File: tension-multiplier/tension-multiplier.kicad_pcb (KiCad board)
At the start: 2 copper layers, 23 x 16 mm, 4 parts, among them J1 Conn_01x03_Pin, J2 Conn_01x02_Pin, J3 Conn_01x02_Pin, U1 AD633ARZ

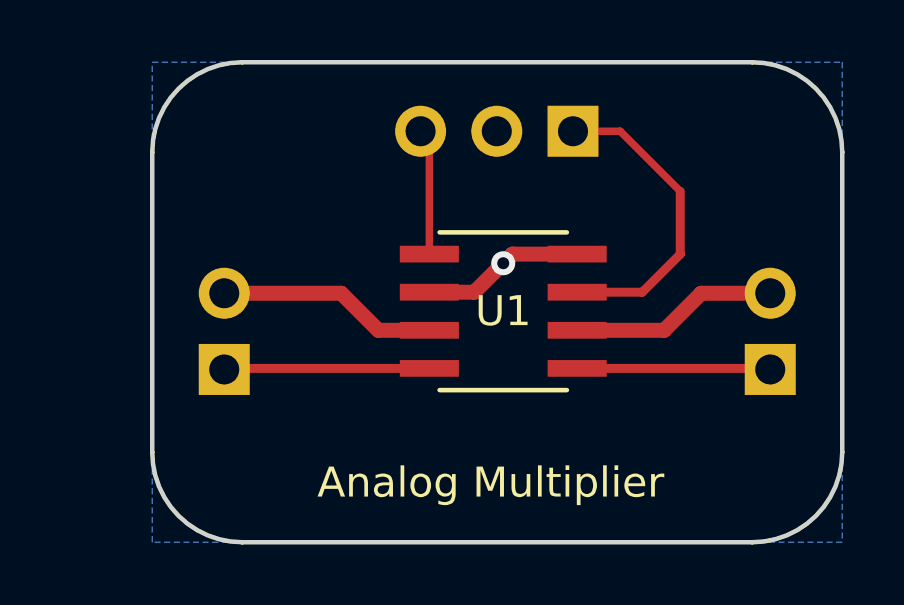
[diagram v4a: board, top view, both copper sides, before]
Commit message: Modifies auxiliary boards
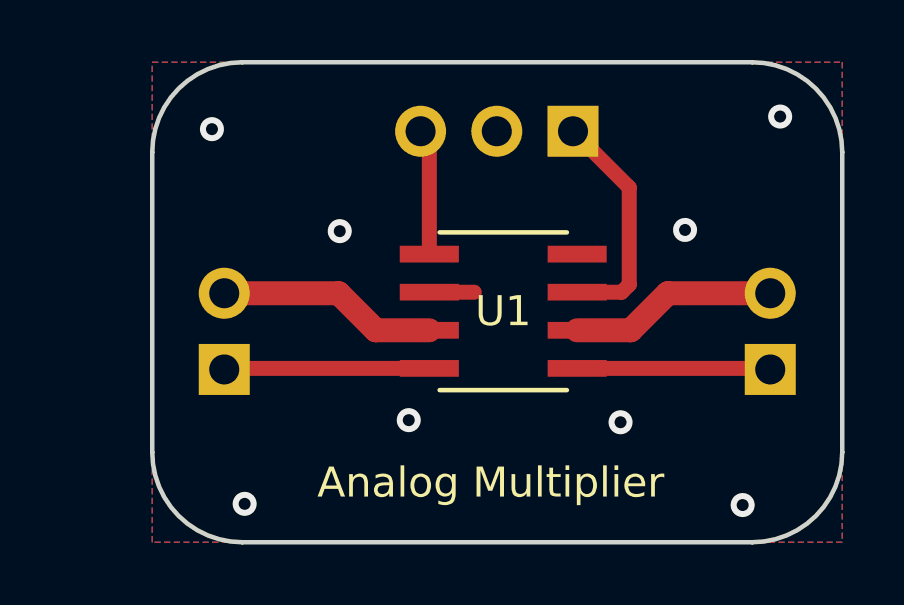
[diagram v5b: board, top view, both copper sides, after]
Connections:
- net VDD renamed +9V
- net VEE renamed -9V
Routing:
- net GND: track 5.76 -> 1.80 mm, vias 1 -> 8
- net Net-(J1-Pin_1): track 10.5 -> 7.73 mm
- added copper zone on F.Cu, net GND
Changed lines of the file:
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@@
       (outputformat 1)
       (mirror false)
-      (drillshape 1)
+      (drillshape 0)
       (scaleselection 1)
-      (outputdirectory "")
+      (outputdirectory "gerber_files")
     )
   )
@@
   (net 3 "Net-(J2-Pin_1)")
   (net 4 "Net-(J3-Pin_1)")
-  (net 5 "VDD")
-  (net 6 "GND")
-  (net 7 "VEE")
+  (net 5 "GND")
+  (net 6 "-9V")
+  (net 7 "+9V")
   (footprint "footprints:R_8_ADI" (layer "F.Cu")
     (at 149.7 88.3)
@@
     (attr smd)
     (fp_text reference "U1" (at 0 0 unlocked) (layer "F.SilkS")
-        (effects (font (size 1 1) (thickness 0.2)))
+        (effects (font (size 1 1) (thickness 0.15)))
     )
     (fp_text value "AD633ARZ" (at 0 0 unlocked) (layer "F.Fab")
-        (effects (font (size 1 1) (thickness 0.2)))
+        (effects (font (size 1 1) (thickness 0.15)))
     )
     (fp_text user "*" (at -2.7178 -3.606 unlocked) (layer "F.SilkS") hide
@@
         (effects (font (size 1 1) (thickness 0.15)))
     )
+    (fp_text user "*" (at -1.6129 -2.4257 unlocked) (layer "F.Fab")
+        (effects (font (size 1 1) (thickness 0.15)))
+    )
+    (fp_text user "*" (at -1.6129 -2.4257 unlocked) (layer "F.Fab")
+        (effects (font (size 1 1) (thickness 0.15)))
+    )
     (fp_text user "${REFERENCE}" (at 0 0 unlocked) (layer "F.Fab")
-        (effects (font (size 1 1) (thickness 0.2) bold))
-    )
-    (fp_text user "*" (at -1.6129 -2.4257 unlocked) (layer "F.Fab")
-        (effects (font (size 1 1) (thickness 0.15)))
-    )
-    (fp_text user "*" (at -1.6129 -2.4257 unlocked) (layer "F.Fab")
         (effects (font (size 1 1) (thickness 0.15)))
     )
@@
       (net 2 "Net-(J1-Pin_3)") (pinfunction "Y1") (pintype "input"))
     (pad "2" smd rect (at -2.4638 -0.635) (size 1.969999 0.558) (layers "F.Cu" "F.Paste" "F.Mask")
-      (net 6 "GND") (pinfunction "Y2") (pintype "input"))
+      (net 5 "GND") (pinfunction "Y2") (pintype "input"))
     (pad "3" smd rect (at -2.4638 0.635) (size 1.969999 0.558) (layers "F.Cu" "F.Paste" "F.Mask")
-      (net 7 "VEE") (pinfunction "-VS") (pintype "power_in"))
+      (net 6 "-9V") (pinfunction "-VS") (pintype "power_in"))
     (pad "4" smd rect (at -2.4638 1.905) (size 1.969999 0.558) (layers "F.Cu" "F.Paste" "F.Mask")
       (net 4 "Net-(J3-Pin_1)") (pinfunction "Z") (pintype "output"))
@@
       (net 3 "Net-(J2-Pin_1)") (pinfunction "W") (pintype "output"))
     (pad "6" smd rect (at 2.4638 0.635) (size 1.969999 0.558) (layers "F.Cu" "F.Paste" "F.Mask")
-      (net 5 "VDD") (pinfunction "+VS") (pintype "power_in"))
+      (net 7 "+9V") (pinfunction "+VS") (pintype "power_in"))
     (pad "7" smd rect (at 2.4638 -0.635) (size 1.969999 0.558) (layers "F.Cu" "F.Paste" "F.Mask")
       (net 1 "Net-(J1-Pin_1)") (pinfunction "X1") (pintype "input"))
     (pad "8" smd rect (at 2.4638 -1.905) (size 1.969999 0.558) (layers "F.Cu" "F.Paste" "F.Mask")
-      (net 6 "GND") (pinfunction "X2") (pintype "input"))
+      (net 5 "GND") (pinfunction "X2") (pintype "input"))
     (model "${KIPRJMOD}/R_8_ADI.step"
       (offset (xyz 0 0 0))
@@
       (net 1 "Net-(J1-Pin_1)") (pinfunction "Pin_1") (pintype "passive"))
     (pad "2" thru_hole oval (at 0 -2.54 90) (size 1.7 1.7) (drill 1) (layers "*.Cu" "*.Mask")
-      (net 6 "GND") (pinfunction "Pin_2") (pintype "passive"))
+      (net 5 "GND") (pinfunction "Pin_2") (pintype "passive"))
     (pad "3" thru_hole oval (at 0 -5.08 90) (size 1.7 1.7) (drill 1) (layers "*.Cu" "*.Mask")
       (net 2 "Net-(J1-Pin_3)") (pinfunction "Pin_3") (pintype "passive"))
@@
       (net 4 "Net-(J3-Pin_1)") (pinfunction "Pin_1") (pintype "passive"))
     (pad "2" thru_hole oval (at 0 -2.54) (size 1.7 1.7) (drill 1) (layers "*.Cu" "*.Mask")
-      (net 7 "VEE") (pinfunction "Pin_2") (pintype "passive"))
+      (net 6 "-9V") (pinfunction "Pin_2") (pintype "passive"))
     (model "${KICAD6_3DMODEL_DIR}/Connector_PinHeader_2.54mm.3dshapes/PinHeader_1x02_P2.54mm_Vertical.wrl"
       (offset (xyz 0 0 0))
@@
       (net 3 "Net-(J2-Pin_1)") (pinfunction "Pin_1") (pintype "passive"))
     (pad "2" thru_hole oval (at 0 -2.54) (size 1.7 1.7) (drill 1) (layers "*.Cu" "*.Mask")
-      (net 5 "VDD") (pinfunction "Pin_2") (pintype "passive"))
+      (net 7 "+9V") (pinfunction "Pin_2") (pintype "passive"))
     (model "${KICAD6_3DMODEL_DIR}/Connector_PinHeader_2.54mm.3dshapes/PinHeader_1x02_P2.54mm_Vertical.wrl"
       (offset (xyz 0 0 0))
@@
   )
   (gr_text "JLCJLCJLCJLC" (at 154 94.6) (layer "B.SilkS")
-    (effects (font (size 0.8 0.8) (thickness 0.15)) (justify left bottom mirror))
+    (effects (font (size 1 1) (thickness 0.15)) (justify left bottom mirror))
   )
   (gr_text "Uw" (at 156.6 90.7) (layer "B.SilkS")
@@
     (effects (font (size 1 1) (thickness 0.2)) (justify left bottom))
   )
-  (segment (start 153.6 82.3) (end 152.025 82.3) (width 0.25) (layer "F.Cu") (net 1))
-  (segment (start 152.1638 87.665) (end 154.335 87.665) (width 0.3) (layer "F.Cu") (net 1))
-  (segment (start 155.6 84.3) (end 153.6 82.3) (width 0.25) (layer "F.Cu") (net 1))
-  (segment (start 155.6 86.4) (end 155.6 84.3) (width 0.3) (layer "F.Cu") (net 1))
-  (segment (start 154.335 87.665) (end 155.6 86.4) (width 0.3) (layer "F.Cu") (net 1))
+  (segment (start 152.1638 87.665) (end 153.648799 87.665) (width 0.5) (layer "F.Cu") (net 1))
+  (segment (start 153.9 84.175) (end 152.025 82.3) (width 0.5) (layer "F.Cu") (net 1))
+  (segment (start 153.648799 87.665) (end 153.9 87.413799) (width 0.5) (layer "F.Cu") (net 1))
+  (segment (start 153.9 87.413799) (end 153.9 84.175) (width 0.5) (layer "F.Cu") (net 1))
   (segment (start 147.2362 82.1912) (end 146.945 81.9) (width 0.3) (layer "F.Cu") (net 2))
   (segment (start 147.1962 81.9762) (end 147.12 81.9) (width 0.3) (layer "F.Cu") (net 2))
-  (segment (start 147.2362 82.5912) (end 146.945 82.3) (width 0.25) (layer "F.Cu") (net 2))
-  (segment (start 147.2362 86.395) (end 147.2362 82.5912) (width 0.25) (layer "F.Cu") (net 2))
-  (segment (start 152.1638 90.205) (end 158.565 90.205) (width 0.3) (layer "F.Cu") (net 3))
-  (segment (start 158.565 90.205) (end 158.6 90.24) (width 0.3) (layer "F.Cu") (net 3))
-  (segment (start 147.2362 90.205) (end 140.435 90.205) (width 0.3) (layer "F.Cu") (net 4))
-  (segment (start 140.435 90.205) (end 140.4 90.24) (width 0.3) (layer "F.Cu") (net 4))
-  (segment (start 152.1638 88.935) (end 155.065 88.935) (width 0.5) (layer "F.Cu") (net 5))
-  (segment (start 156.3 87.7) (end 158.6 87.7) (width 0.5) (layer "F.Cu") (net 5))
-  (segment (start 155.065 88.935) (end 156.3 87.7) (width 0.5) (layer "F.Cu") (net 5))
-  (segment (start 148.735 87.665) (end 149.7 86.7) (width 0.5) (layer "F.Cu") (net 6))
-  (segment (start 147.2362 87.665) (end 148.735 87.665) (width 0.5) (layer "F.Cu") (net 6))
-  (segment (start 152.1638 86.395) (end 150.005 86.395) (width 0.5) (layer "F.Cu") (net 6))
-  (segment (start 150.005 86.395) (end 149.7 86.7) (width 0.5) (layer "F.Cu") (net 6))
-  (via (at 149.7 86.7) (size 0.8) (drill 0.4) (layers "F.Cu" "B.Cu") (net 6))
-  (segment (start 149.7 82.115) (end 149.485 81.9) (width 0.5) (layer "B.Cu") (net 6))
-  (segment (start 144.3 87.7) (end 145.535 88.935) (width 0.5) (layer "F.Cu") (net 7))
-  (segment (start 140.4 87.7) (end 144.3 87.7) (width 0.5) (layer "F.Cu") (net 7))
-  (segment (start 145.535 88.935) (end 147.2362 88.935) (width 0.5) (layer "F.Cu") (net 7))
-  (zone (net 6) (net_name "GND") (layer "B.Cu") (hatch edge 0.5)
+  (segment (start 147.2362 86.395) (end 147.2362 82.5912) (width 0.5) (layer "F.Cu") (net 2))
+  (segment (start 147.2362 82.5912) (end 146.945 82.3) (width 0.5) (layer "F.Cu") (net 2))
+  (segment (start 158.565 90.205) (end 158.6 90.24) (width 0.5) (layer "F.Cu") (net 3))
+  (segment (start 152.1638 90.205) (end 158.565 90.205) (width 0.5) (layer "F.Cu") (net 3))
+  (segment (start 140.435 90.205) (end 140.4 90.24) (width 0.5) (layer "F.Cu") (net 4))
+  (segment (start 147.2362 90.205) (end 140.435 90.205) (width 0.5) (layer "F.Cu") (net 4))
+  (segment (start 147.2362 87.665) (end 148.735 87.665) (width 0.5) (layer "F.Cu") (net 5))
+  (via (at 144.25 85.63) (size 0.8) (drill 0.4) (layers "F.Cu" "B.Cu") (free) (net 5))
+  (via (at 153.61 92) (size 0.8) (drill 0.4) (layers "F.Cu" "B.Cu") (free) (net 5))
+  (via (at 139.99 82.23) (size 0.8) (drill 0.4) (layers "F.Cu" "B.Cu") (free) (net 5))
+  (via (at 158.93 81.81) (size 0.8) (drill 0.4) (layers "F.Cu" "B.Cu") (free) (net 5))
+  (via (at 141.08 94.72) (size 0.8) (drill 0.4) (layers "F.Cu" "B.Cu") (free) (net 5))
+  (via (at 157.68 94.76) (size 0.8) (drill 0.4) (layers "F.Cu" "B.Cu") (free) (net 5))
+  (via (at 155.76 85.59) (size 0.8) (drill 0.4) (layers "F.Cu" "B.Cu") (free) (net 5))
+  (via (at 146.55 91.93) (size 0.8) (drill 0.4) (layers "F.Cu" "B.Cu") (free) (net 5))
+  (segment (start 149.7 82.115) (end 149.485 81.9) (width 0.5) (layer "B.Cu") (net 5))
+  (segment (start 147.2362 88.935) (end 145.451201 88.935) (width 0.8) (layer "F.Cu") (net 6))
+  (segment (start 145.451201 88.935) (end 144.216201 87.7) (width 0.8) (layer "F.Cu") (net 6))
+  (segment (start 144.216201 87.7) (end 140.4 87.7) (width 0.8) (layer "F.Cu") (net 6))
+  (segment (start 153.948799 88.935) (end 155.183799 87.7) (width 0.8) (layer "F.Cu") (net 7))
+  (segment (start 155.183799 87.7) (end 158.6 87.7) (width 0.8) (layer "F.Cu") (net 7))
+  (segment (start 152.1638 88.935) (end 153.948799 88.935) (width 0.8) (layer "F.Cu") (net 7))
+  (zone (net 5) (net_name "GND") (layer "F.Cu") (hatch edge 0.5)
     (connect_pads (clearance 0.3))
     (min_thickness 0.25) (filled_areas_thickness no)
+    (fill yes (thermal_gap 0.5) (thermal_bridge_width 0.5))
+    (polygon
+      (pts
+        (xy 138 80)
+        (xy 161 80)
+        (xy 161 96)
+        (xy 138 96)
+      )
+    )
+  )
+  (zone (net 5) (net_name "GND") (layer "B.Cu") (hatch edge 0.5)
+    (connect_pads (clearance 0.3))
+    (min_thickness 0.25) (filled_areas_thickness no)
